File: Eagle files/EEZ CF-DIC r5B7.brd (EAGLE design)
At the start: 155 x 90 mm, 273 parts, among them IC1 VIPer35L, IC2 SI8233BB-D-IS1, IC3 LM5041B, IC4 LM258D, IC5 IR11688STRPBF, IC6 LM258D, IC7 TL103W, P1 T910W-50K, Q1 MMBT5551, Q2 C3M0280090D, Q3 C3M0280090D, Q4 NYC0102BLT1G, Q5 IRFP4332PBF, Q6 IRFP4332PBF, Q7 FDD86250-F085, Q8 FDD86250-F085, X1 39-30-3035, X2 22-05-7095, X3 B2B-ZR, X4 39-30-1020

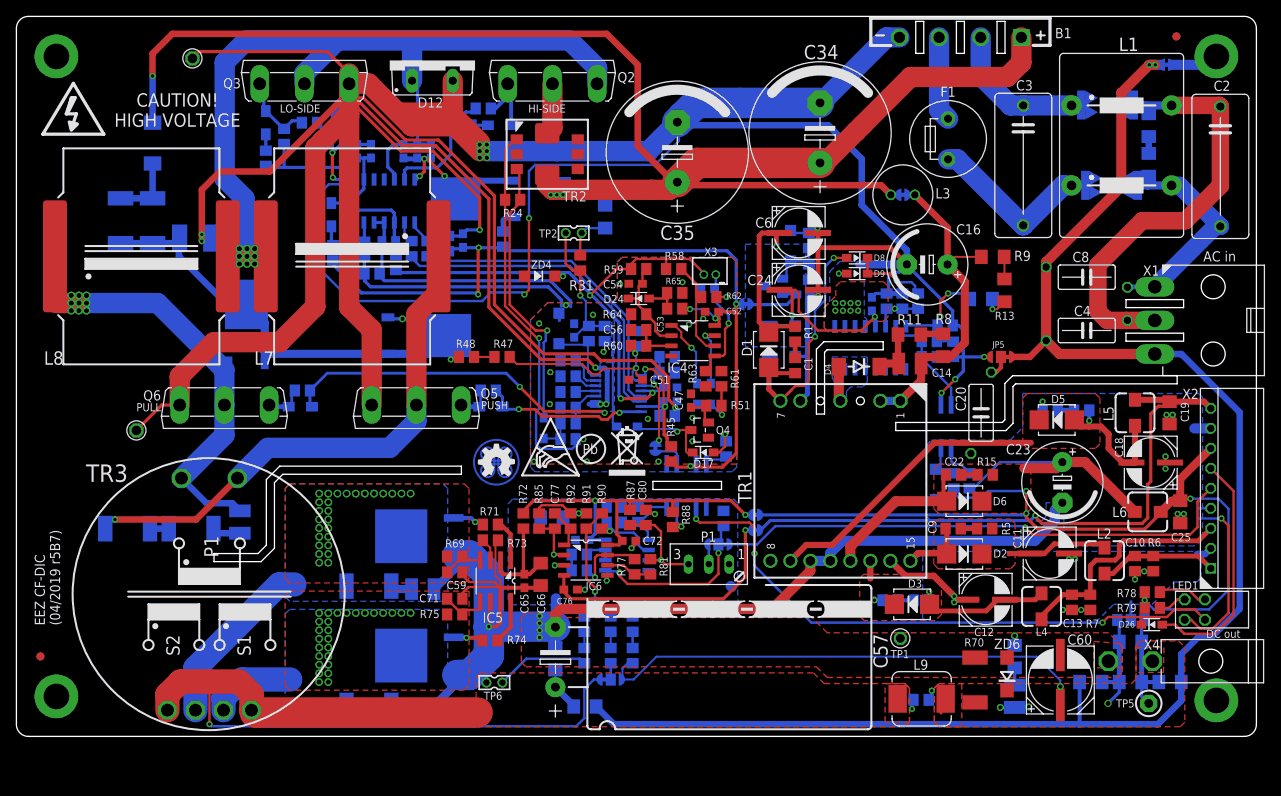
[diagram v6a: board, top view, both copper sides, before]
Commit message: new LED1 and primary side snubbers
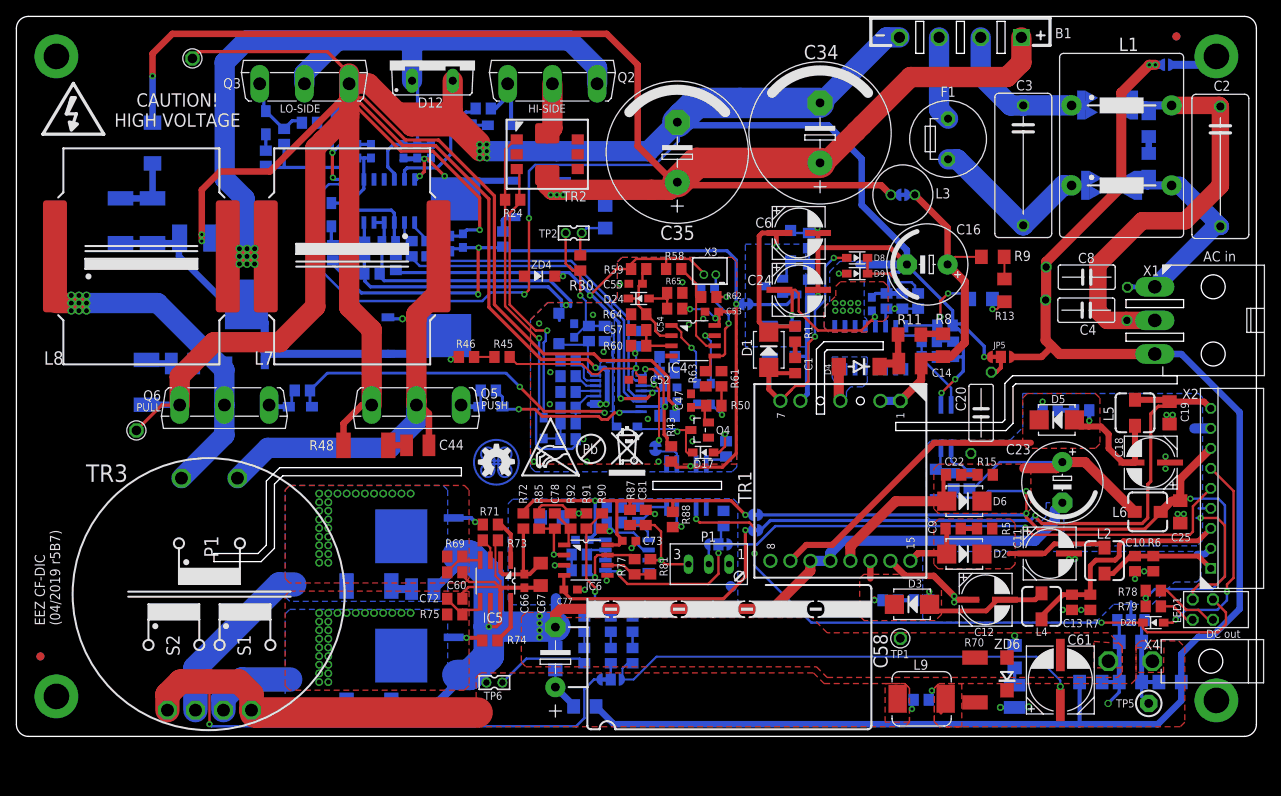
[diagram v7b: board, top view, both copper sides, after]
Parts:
- added C82: N.C., rcl:C0805
- C4: device EEZ_Lib1:CY075-032X103-ROTATED -> EEZ_Lib1:CY075-032X103
- C41: value 2n2/1kV -> 100n/500V; device rcl:C1210 -> rcl:C1812
- C42: value 100n/500V -> 100n; device rcl:C1812 -> rcl:C0603
- C43, C54: value 100n -> 1u; device rcl:C0603 -> rcl:C0805
- C44: value 1u -> 2n2/1kV; device rcl:C0805 -> rcl:C1210
- C48: value 100n -> 2n2/1kV; device rcl:C0603 -> rcl:C1210
- C49: value 470p -> 100n; device rcl:C0805 -> rcl:C0603
- C51: value 10n -> 470p; device rcl:C0603 -> rcl:C0805
- C52: value 100n -> 10n
- C53: value 1u -> 100n; device rcl:C0805 -> rcl:C0603
- C55: value N.C. -> 100n
- C56: value 1u -> N.C.; device rcl:C0805 -> rcl:C0603
- C57: value UVZ1J222MHD -> 1u; device EEZ_Lib1:ECAP7.5/18-H35.5A -> rcl:C0805
- C58: value 1u/100V -> UVZ1J222MHD; device rcl:C1206 -> EEZ_Lib1:ECAP7.5/18-H35.5A
- C59: value 47p/200V -> 1u/100V; device rcl:C0805 -> rcl:C1206
- C60: value HHXC630ARA330MHA0G -> 47p/200V; device EEZ_Lib1:CAPAE830X1050N -> rcl:C0805
- C61: value 1u/100V -> HHXC630ARA330MHA0G; device rcl:C1206 -> EEZ_Lib1:CAPAE830X1050N
- C62: value 100n/100V -> 1u/100V
- C63, C70: value 2n2/1kV -> 100n/100V; device rcl:C1210 -> rcl:C1206
- C64: value N.C. -> 2n2/1kV; device rcl:C1206 -> rcl:C1210
- C65: value 100n -> N.C.; device rcl:C0603 -> rcl:C1206
- C66: value 4u7 -> 100n; device rcl:C1206 -> rcl:C0603
- C67: value 4n7/200V -> 4u7
- C68: value 4n7/200V -> N.C.
- C69: value 4n7/200V -> 100n/100V
- C71: value 47p/200V -> 2n2/1kV; device rcl:C0805 -> rcl:C1210
- C72, C76: value 100n -> 47p/200V; device rcl:C0603 -> rcl:C0805
- C73: value 2n2 -> 100n; device rcl:C0805 -> rcl:C0603
- C74: value 100n -> 4n7; device rcl:C0603 -> rcl:C0805
- C75: value 47p/200V -> 100n; device rcl:C0805 -> rcl:C0603
- C77: value 100p -> 100n; device rcl:C0805 -> rcl:C0603
- C78: value 1n -> 100p
- C79: value N.C. -> 1n; device EEZ_Lib1:EC1206 -> rcl:C0805
- C80: value 1u -> N.C.; device rcl:C0805 -> EEZ_Lib1:EC1206
- C81: value N.C. -> 1u
- JP2: value JP2-NOCUT -> JP2-CUT; device EEZ_Lib1:JP2-NOCUT -> EEZ_Lib1:JP2-CUT
- LED1: value L-934EB/1Y1ID-RV -> WP934MD/LYLID; device EEZ_Lib1:L-934EB -> EEZ_Lib1:WP934MD
- R30: value 22R/2-3W -> 86K6; device rcl:R2512 -> rcl:R0805
- R31, R47: value 86K6 -> 10R
- R32: value 10R -> 30K
- R33: value 22R/2-3W -> 1R; device rcl:R2512 -> rcl:R0805
- R34: value 30K -> 10R
- R35: value 1R -> 10R
- R36: value 10R -> N.C.
- R37: value 10R -> 47K
- R38: value N.C. -> 1R
- R39: value 47K -> 22R/2-3W; device rcl:R0805 -> rcl:R2512
- R40: value 1R -> 1K
- R41: value 22R/2-3W -> N.C.
- R43: value N.C. -> 10R; device rcl:R2512 -> rcl:R0805
- R44: value 1K -> 8K2
- R45: value 10R -> 86K6
- R46: value 8K2 -> 86K6
- R48: value 86K6 -> 47R/2-3W; device rcl:R0805 -> rcl:R2512
- R49: value 10R -> 15K
- R50: value 15K -> 4K7
- R51: value 4K7 -> 68K
- R52: value 68K -> 220R
- R54: value 220R -> 47R/2-3W; device rcl:R0805 -> rcl:R2512
- R83: value 4K7 -> 1K
- R86: value 27K -> 86K6
- moved C63 89.2 mm to (139.3, 6.79), turned to 0 degrees
- moved C70 83.5 mm to (134.3, 6.79), turned to 0 degrees
- moved C60 76.9 mm to (54.8, 20.5), turned to 180 degrees
- moved C64 74.5 mm to (50.8, 18.4), turned to 180 degrees
- moved C68 73.2 mm to (71.1, 3.75)
- moved R43 71.1 mm to (81.9, 35.3), flipped to the top, turned to 270 degrees
- moved R30 65.6 mm to (70.5, 59.2), flipped to the top, turned to 270 degrees
- moved C65 62.0 mm to (124.8, 9.97), flipped to the bottom
- moved C48 61.0 mm to (20.8, 46.6), turned to 180 degrees
- moved R40 59.0 mm to (88.7, 35.9)
- moved R54 53.0 mm to (16.3, 44.3), turned to 270 degrees
- moved C42 48.8 mm to (69.7, 50.7), turned to 90 degrees
- moved C57 42.2 mm to (77.8, 50.8), turned to 0 degrees
- moved R33 39.1 mm to (44.5, 57.8)
- moved C41 35.9 mm to (22.4, 62.3), turned to 0 degrees
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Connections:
- removed net N$17: C41.1, R33.1
- removed net N$74: OK3.3
- new net N$68: C44.1, R48.1
- net +12V: now also C54.1, R35.2, R43.2; no longer C52.1, R37.2, R45.2
- net +2.5VREF: now also C81.1; no longer C80.1
- net +5VREF: now also C49.2, R31.1; no longer C48.2, R32.1
- net 0V: now also C41.1, C43.2, JP5.NC, R37.2, R38.1, R38.2, R48.2, R54.2; no longer C42.1, C44.2, JP5.NO, R39.2, R40.1, R40.2
- net AGND: now also C42.2, C51.1, C53.2, C55.2, C57.1, OK3.3, R32.1, R33.1, R33.2, R44.2, R49.2, R51.2; no longer C43.2, C48.1, C51.2, C54.2, C55.1, R34.1, R35.1, R35.2, R46.2, R50.2, R52.2
- net CLAMP_C: now also C41.2, R39.1, R46.2; no longer C42.2, R43.1, R48.2
- net COMP: now also C50.2; no longer C49.2
- net FB: now also C52.1, R45.1; no longer C51.1, R47.1
- net GND: now also C58.-, C59.2, C60.1, C61.-, C64.2, C65.1, C67.2, C70.1, C71.2, C72.1, C73.2, C75.2, C77.2, C80.-, C82.2; no longer C57.-, C58.2, C59.1, C60.-, C61.2, C64.1, C65.2, C69.1, C70.2, C71.1, C72.2, C74.2, C76.2, C79.-, C80.2
- net LO_OUT: now also R34.1; no longer R38.1
- net L_PULL: now also C48.2; no longer C41.2
- net L_PUSH: now also C44.2; no longer R30.2
- net N$10: now also C76.2; no longer C75.2
- net N$100: now also R50.1; no longer R51.1
- net N$13: now also R47.1; no longer R49.1
- net N$130: now also R40.2; no longer R42.2
- net N$134: now also C78.1; no longer C77.1
- net N$19: now also R51.1; no longer R52.1
- net N$2: now also R30.1; no longer R31.1
- net N$22: now also R49.1; no longer R50.1
- net N$25: now also R42.1; no longer R44.1
- net N$28: now also C74.2; no longer C73.2
- net N$29: now also R34.2, R37.1; no longer R36.2, R39.1
- net N$30: now also R45.2, R46.1; no longer R47.2, R48.1
- net N$32: now also R40.1; no longer R42.1
- net N$34: now also C57.2; no longer C56.2
- net N$35: now also R39.2; no longer R43.2
- net N$37: now also C51.2, R52.2; no longer C50.2, R54.2
- net N$39: now also C77.1; no longer C76.1
- net N$42: now also C56.2; no longer C55.2
- net N$46: now also C73.1, C75.1; no longer C72.1, C74.1
- net N$48: now also R32.2; no longer R34.2
- net N$5: now also C48.1, R54.1; no longer R30.1, R33.2
- net N$51: now also R50.2; no longer R51.2
- net N$52: now also R36.2; no longer R38.2
- net N$54: now also C43.1, R43.1; no longer C44.1, R45.1
- net N$56: now also R52.1; no longer R54.1
- net N$57: now also C82.1; no longer C81.1
- net N$59: now also C54.2; no longer C53.2
- net N$63: now also R35.1; no longer R37.1
- net N$64: now also C78.2; no longer C77.2
- net N$66: now also C71.1; no longer C70.1
- net N$67: now also C64.1; no longer C63.1
- net N$7: now also C55.1; no longer C54.1
- net N$71: now also C74.1; no longer C73.1
- net N$76: now also C76.1, C79.1; no longer C75.1, C78.1
- net N$8: now also C65.2; no longer C64.2
- net N$9: now also C79.2; no longer C78.2
- net NFB_OFFSET: now also C80.+; no longer C79.+
- net PE: now also C70.2, JP5.NO; no longer C67.2, JP5.NC
- net POUT+: now also C58.+, C59.1, C68.1; no longer C57.+, C58.1, C67.1
- net PREG_OUT+: now also C61.+, C63.1, C69.1; no longer C60.+, C61.1, C68.1
- net PUSH: now also R47.2; no longer R49.2
- net REF: now also R31.2; no longer R32.2
- net SYNC_VCC: now also C67.1; no longer C65.1
- net UVLO: now also C42.1, R30.2, R42.2, R44.1; no longer C43.1, R31.2, R44.2, R46.1
- net VD1: now also C60.2; no longer C59.2
- net VD2: now also C72.2; no longer C71.2
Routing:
- net 0V: track 627.6 -> 643.2 mm
- net L_PUSH: track 70.6 -> 56.8 mm, vias 2 -> 1
- net L_PULL: track 68.0 -> 61.0 mm
- net !FAULT: track 75.4 -> 80.9 mm
- net GND: track 208.3 -> 203.5 mm
- net N$17: track 3.53 -> 0.00 mm
- net V+: track 107.5 -> 104.6 mm
- net N$1: track 29.9 -> 27.1 mm, vias 0 -> 2
- net N$68: track 0.00 -> 2.28 mm
- net N$16: track 6.28 -> 8.02 mm
- net N$11: track 3.53 -> 4.66 mm
- net N$5: track 2.34 -> 3.34 mm
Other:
- outline, holes or cut-outs redrawn
